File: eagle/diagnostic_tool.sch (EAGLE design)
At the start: 9 parts, among them T1 PT204-6C

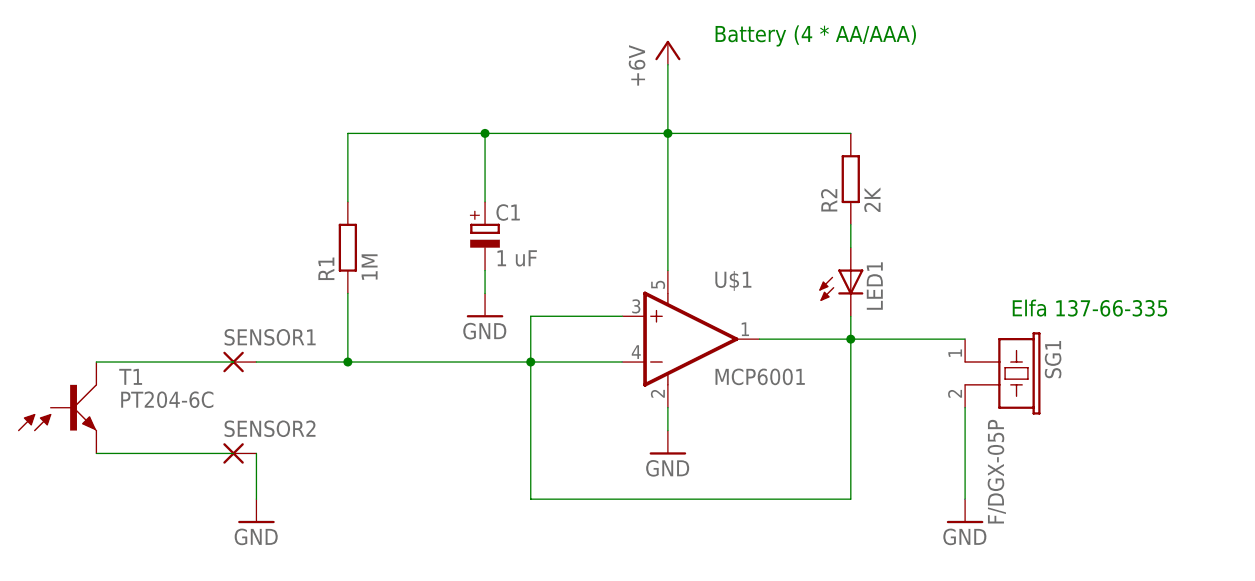
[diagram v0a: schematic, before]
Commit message: Fixed buffer amp.
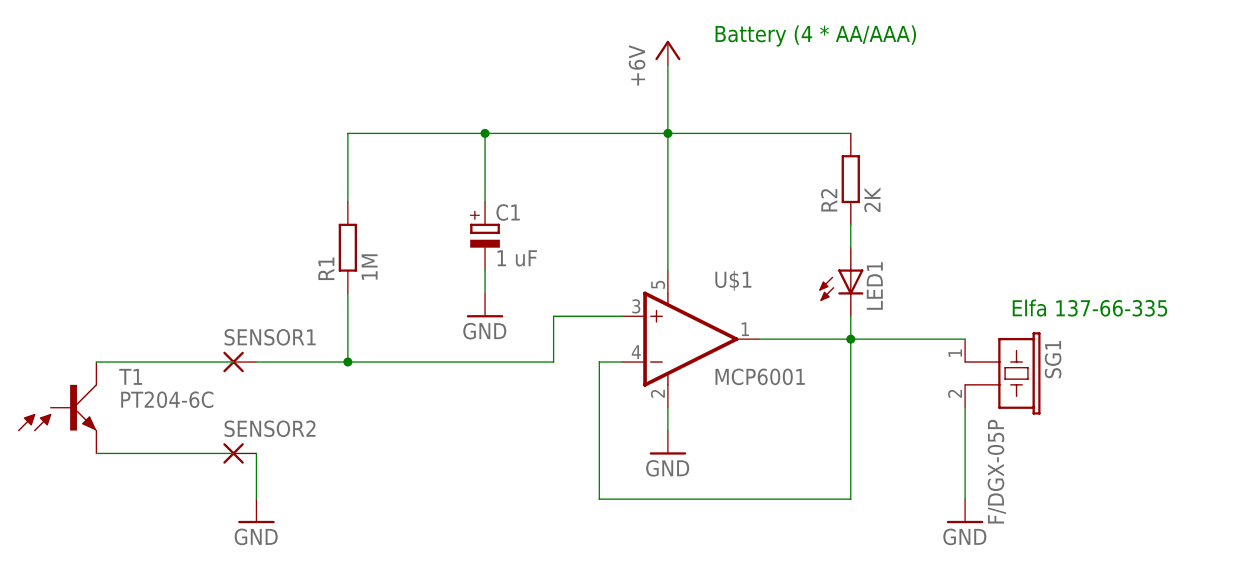
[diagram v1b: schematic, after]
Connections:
- new net N$5: R1.1, SENSOR1.P, U$1.+IN
- net N$3: no longer R1.1, SENSOR1.P, U$1.+IN
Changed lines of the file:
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@@
 <wire x1="114.3" y1="111.76" x2="114.3" y2="109.22" width="0.1524" layer="91"/>
 <junction x="114.3" y="109.22"/>
+<wire x1="86.36" y1="91.44" x2="114.3" y2="91.44" width="0.1524" layer="91"/>
+<wire x1="114.3" y1="109.22" x2="114.3" y2="91.44" width="0.1524" layer="91"/>
+<pinref part="SG1" gate="G$1" pin="1"/>
 <pinref part="U$1" gate="G$1" pin="-IN"/>
-<wire x1="88.9" y1="106.68" x2="78.74" y2="106.68" width="0.1524" layer="91"/>
-<wire x1="78.74" y1="106.68" x2="78.74" y2="91.44" width="0.1524" layer="91"/>
-<wire x1="78.74" y1="91.44" x2="114.3" y2="91.44" width="0.1524" layer="91"/>
-<pinref part="U$1" gate="G$1" pin="+IN"/>
-<wire x1="88.9" y1="111.76" x2="78.74" y2="111.76" width="0.1524" layer="91"/>
-<wire x1="78.74" y1="111.76" x2="78.74" y2="106.68" width="0.1524" layer="91"/>
-<junction x="78.74" y="106.68"/>
-<wire x1="78.74" y1="106.68" x2="58.42" y2="106.68" width="0.1524" layer="91"/>
-<pinref part="R1" gate="G$1" pin="1"/>
-<wire x1="58.42" y1="114.3" x2="58.42" y2="106.68" width="0.1524" layer="91"/>
-<wire x1="114.3" y1="109.22" x2="114.3" y2="91.44" width="0.1524" layer="91"/>
-<wire x1="58.42" y1="106.68" x2="48.26" y2="106.68" width="0.1524" layer="91"/>
-<junction x="58.42" y="106.68"/>
-<pinref part="SENSOR1" gate="G$1" pin="P"/>
-<pinref part="SG1" gate="G$1" pin="1"/>
+<wire x1="88.9" y1="106.68" x2="86.36" y2="106.68" width="0.1524" layer="91"/>
+<wire x1="86.36" y1="106.68" x2="86.36" y2="91.44" width="0.1524" layer="91"/>
 </segment>
 </net>
@@
 </segment>
 </net>
+<net name="N$5" class="0">
+<segment>
+<pinref part="U$1" gate="G$1" pin="+IN"/>
+<wire x1="88.9" y1="111.76" x2="81.28" y2="111.76" width="0.1524" layer="91"/>
+<wire x1="81.28" y1="111.76" x2="81.28" y2="106.68" width="0.1524" layer="91"/>
+<wire x1="81.28" y1="106.68" x2="58.42" y2="106.68" width="0.1524" layer="91"/>
+<pinref part="R1" gate="G$1" pin="1"/>
+<wire x1="58.42" y1="114.3" x2="58.42" y2="106.68" width="0.1524" layer="91"/>
+<junction x="58.42" y="106.68"/>
+<wire x1="58.42" y1="106.68" x2="48.26" y2="106.68" width="0.1524" layer="91"/>
+<pinref part="SENSOR1" gate="G$1" pin="P"/>
+</segment>
+</net>
